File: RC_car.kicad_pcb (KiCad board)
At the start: 2 copper layers, 36 parts, among them J1 nRF24L01, J10 MP1584_5V_IN-, J11 MP1584_IN+, J12 MP1584_IN-, J13 MP1584_OUT-, J14 MP1584_OUT+, J2 MOTOR, J3 BATTERY_12V, J4 SERVO, J5 I2C, J7 MP1584_5V_IN+, J8 MP1584_5V_OUT+, J9 MP1584_5V_OUT-, U2 L298N, U3 LM2596T-5

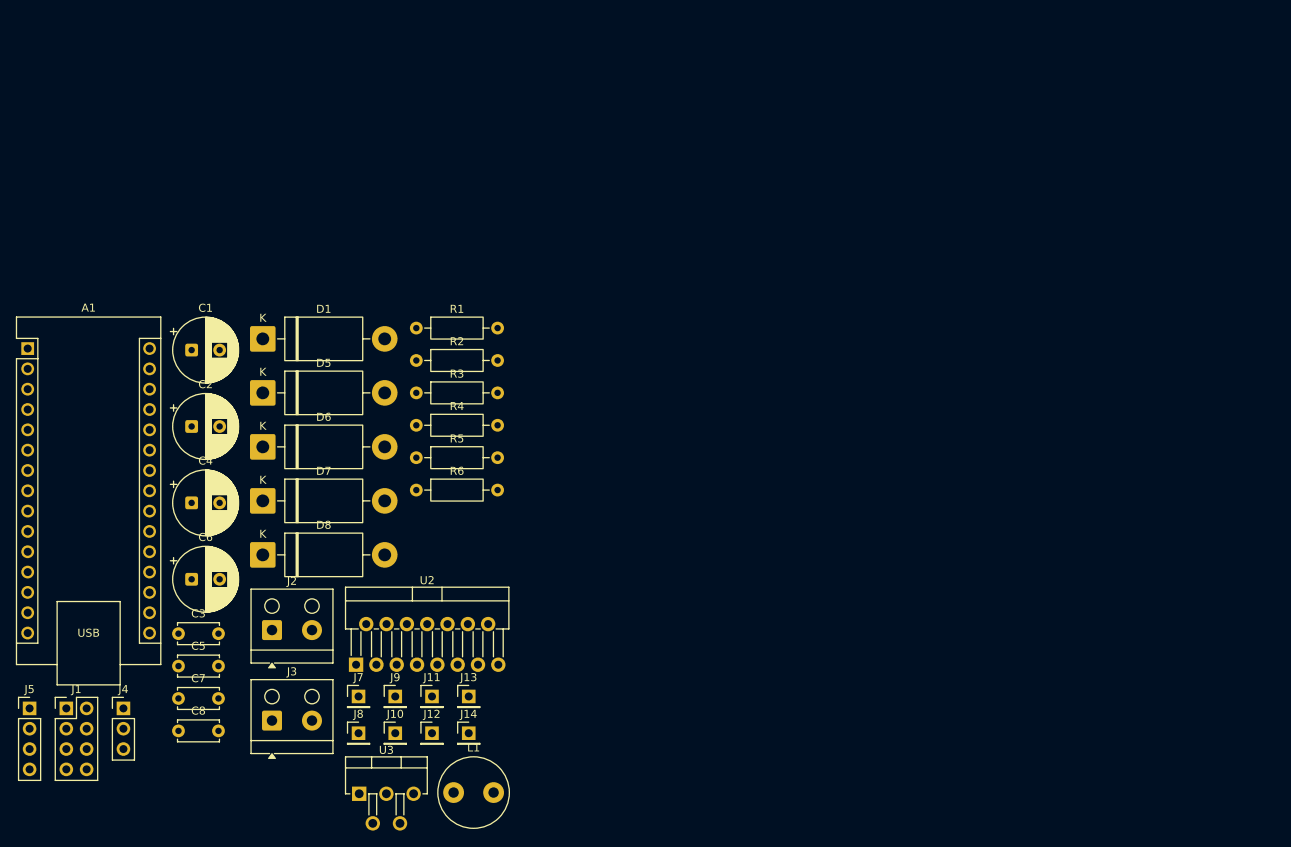
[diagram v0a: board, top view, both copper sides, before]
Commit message: PCB placement: power/logic zone separation, beta vision of the pcb layout
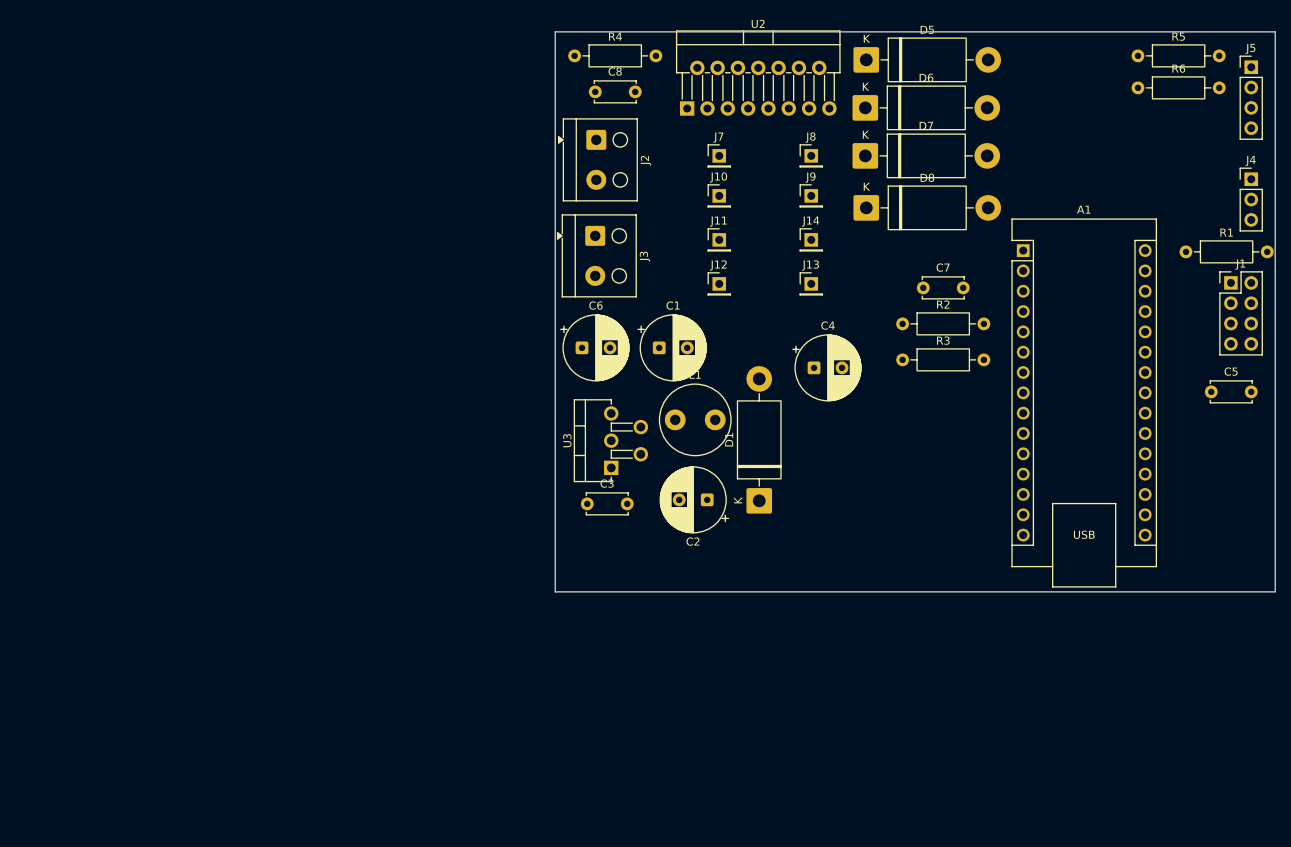
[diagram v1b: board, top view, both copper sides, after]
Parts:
- moved J5 172.5 mm to (278.0, 40.4)
- moved J4 155.7 mm to (278.0, 54.4)
- moved J1 155.0 mm to (275.5, 67.4)
- moved C5 133.6 mm to (273.0, 81.0)
- moved A1 125.0 mm to (249.5, 63.3)
- moved C7 106.3 mm to (237.0, 68.0)
- moved R6 103.3 mm to (263.8, 43.0)
- moved R5 103.2 mm to (263.8, 39.0)
- moved R1 96.7 mm to (269.8, 63.5)
- moved C8 95.4 mm to (196.0, 43.5)
- moved J8 91.7 mm to (223.0, 51.5)
- moved D8 87.0 mm to (229.9, 58.0)
- moved D7 86.8 mm to (229.8, 51.5)
- moved D6 86.4 mm to (229.8, 45.5)
- moved D5 86.2 mm to (229.9, 39.5)
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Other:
- board outline added: 90 x 70 mm

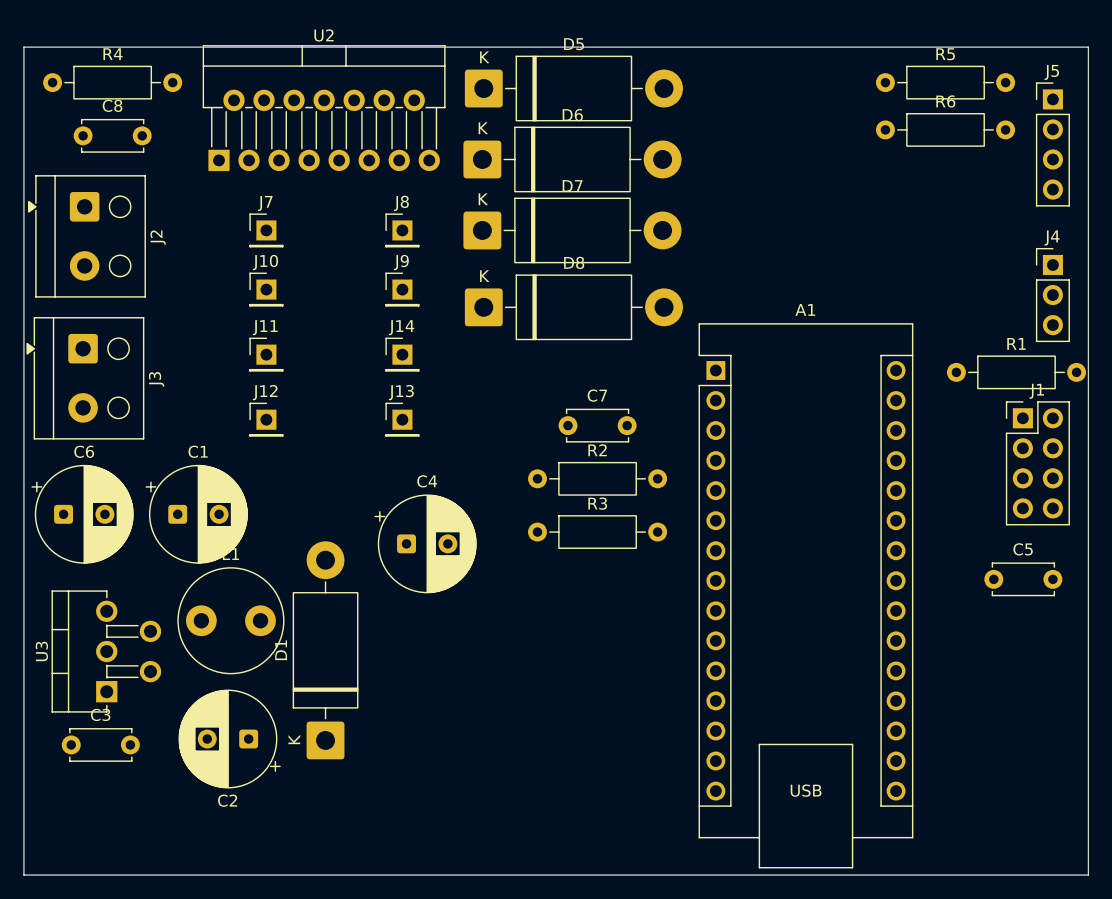
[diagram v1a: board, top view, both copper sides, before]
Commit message: PCB routing: power rails and I2C/signal traces
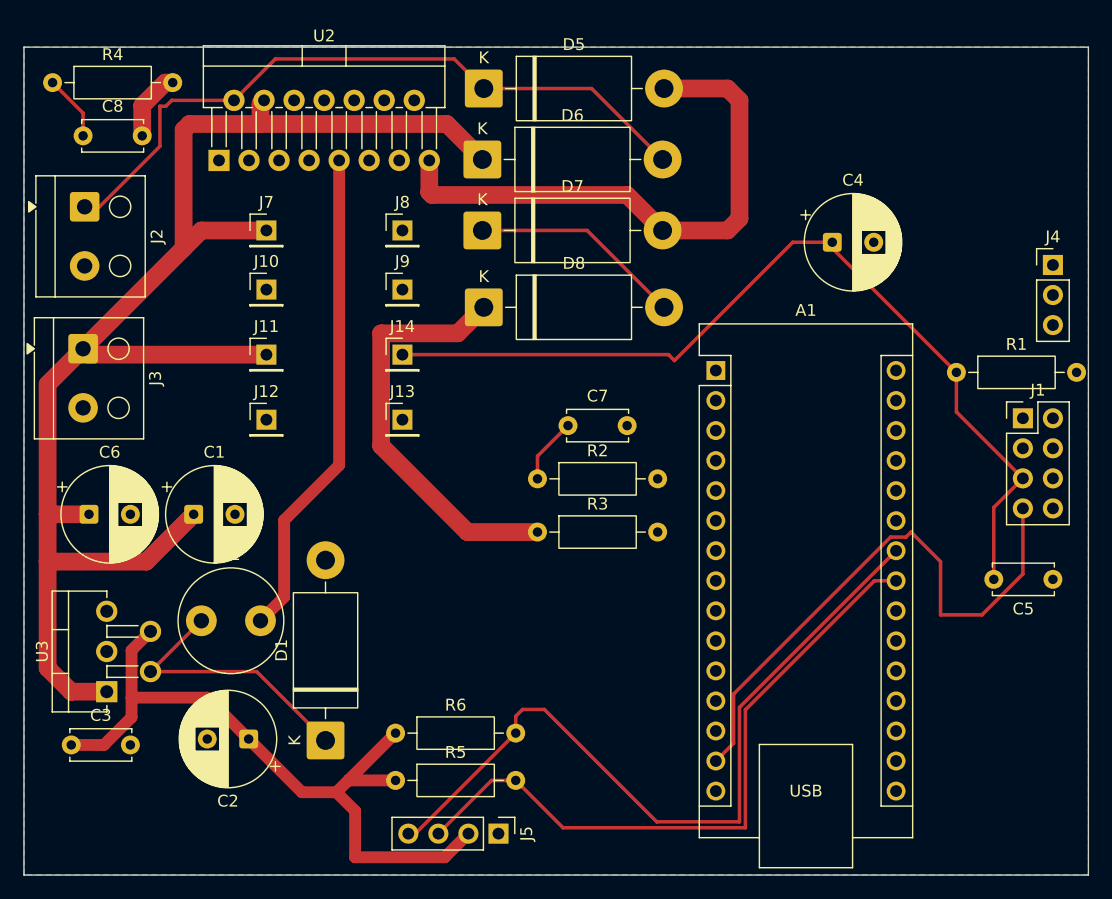
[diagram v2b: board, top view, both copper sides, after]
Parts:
- moved J5 77.8 mm to (231.1, 102.5), turned to -90 degrees
- moved R5 72.1 mm to (222.4, 98.0)
- moved R6 65.7 mm to (222.4, 94.0)
- moved C4 44.1 mm to (259.3, 52.5)
- moved C5 5.00 mm to (278.0, 81.0), turned to 180 degrees
- moved C6 2.15 mm to (196.5, 75.5)
- moved C1 1.35 mm to (205.3, 75.5)
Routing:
- net Net-(D6-K): track 0.00 -> 161.1 mm
- net +5V: track 0.00 -> 103.9 mm
- net Net-(J1-Pin_b1): track 0.00 -> 76.9 mm
- net Net-(A1-A5): track 0.00 -> 65.7 mm
- net Net-(D5-K): track 0.00 -> 59.5 mm
- net Net-(A1-A4): track 0.00 -> 56.7 mm
- net GND: track 0.00 -> 53.4 mm
- net Net-(A1-D11): track 0.00 -> 48.9 mm
- net Net-(D1-K): track 0.00 -> 23.7 mm
- net Net-(D7-K): track 0.00 -> 18.1 mm
- net Net-(A1-A1): track 0.00 -> 5.57 mm
- net Net-(A1-A0): track 0.00 -> 5.57 mm
- added copper zone on B.Cu, net GND
